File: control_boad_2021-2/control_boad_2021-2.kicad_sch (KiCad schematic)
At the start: 29 parts, among them J1 Conn_01x10_Female, J2 Conn_01x10_Female, J3 USB_C_Receptacle_PowerOnly_6P, J4 USB_C_Receptacle_PowerOnly_6P, J5 Conn_01x03_Female, U1 ESP32-DevKitC, U2 IM920s

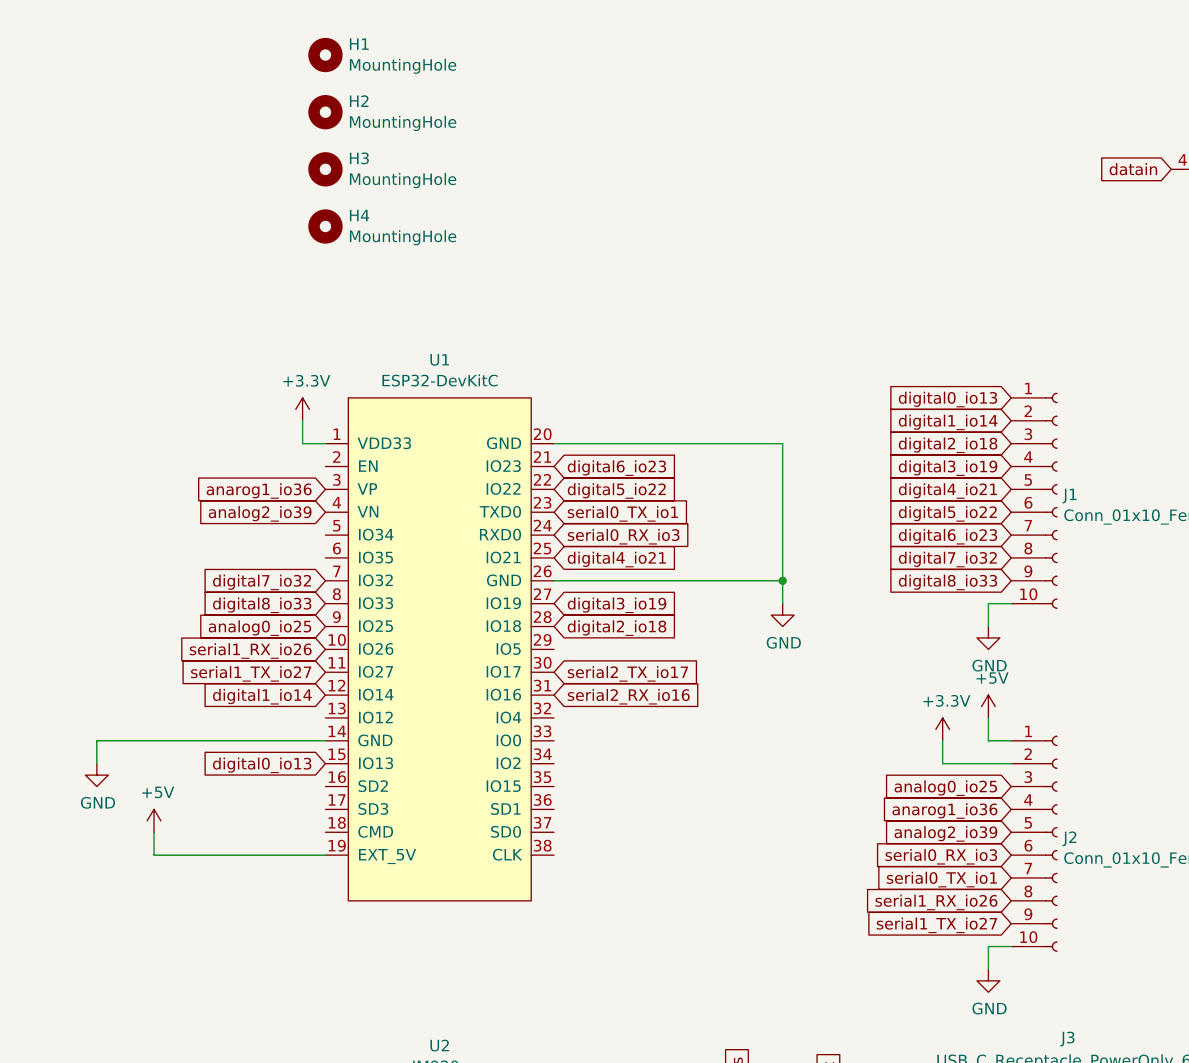
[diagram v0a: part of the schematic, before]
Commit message: replace esp32devkitc to doit esp32devkit v1
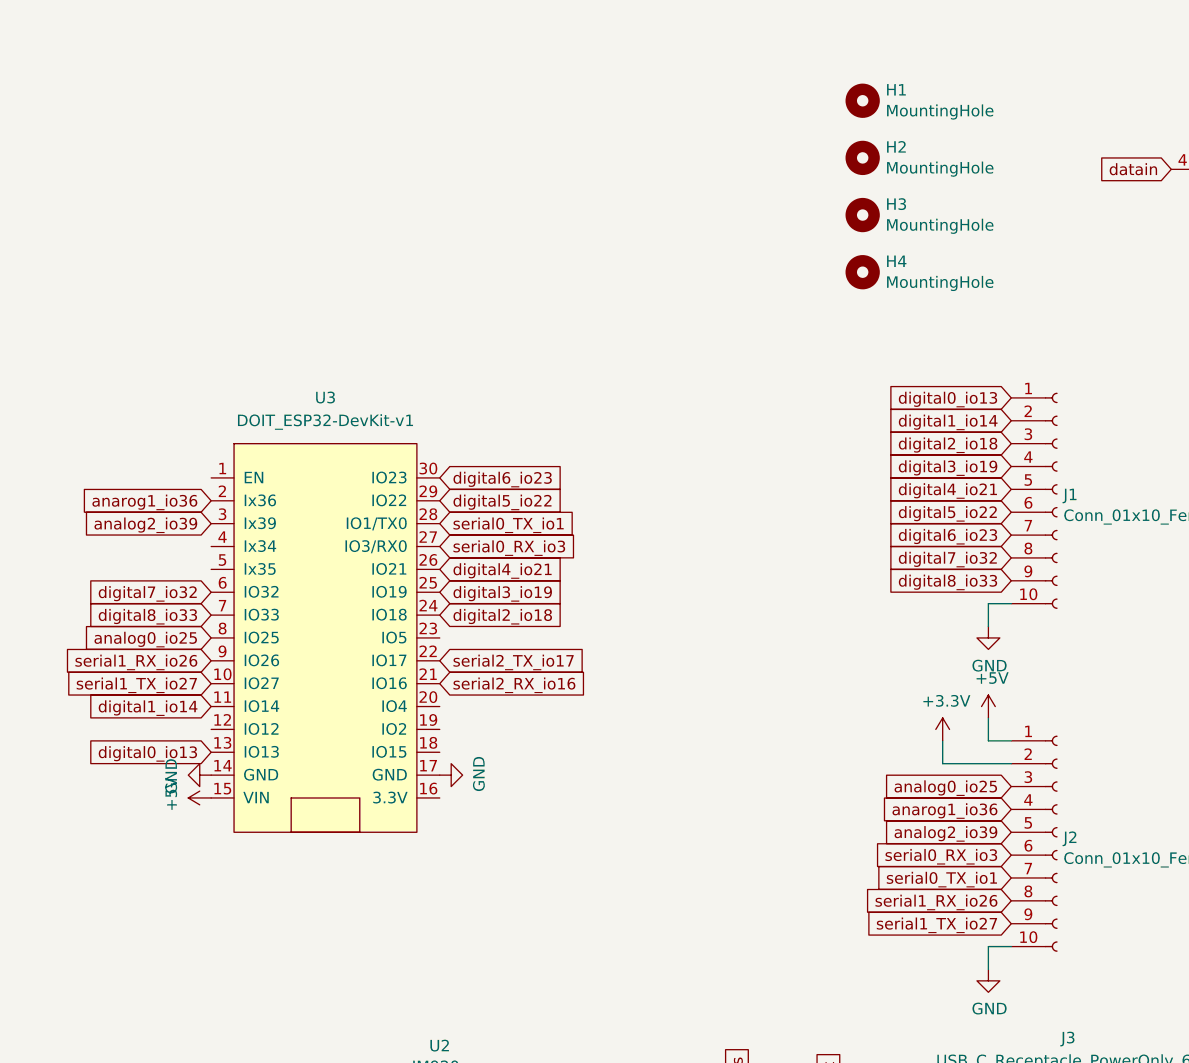
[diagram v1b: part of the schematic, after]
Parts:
- removed U1: ESP32-DevKitC, Boad_dev:ESP32-DevKitC, symbol Boad_dev:ESP32-DevKitC
- added U3: DOIT_ESP32-DevKit-v1, Boad_dev:DOIT_ESP32-DevKit-v1, symbol Boad_dev:DOIT_ESP32-DevKit-v1
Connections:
- net +5V: now also U3.15 (VIN)
- net GND: now also U3.14 (GND), U3.17 (GND)
- net analog0_io25: now also U3.8 (IO25)
- net analog2_io39: now also U3.3 (Ix39)
- net anarog1_io36: now also U3.2 (Ix36)
- net datain: now also U3.9 (IO26)
- net digital0_io13: now also U3.13 (IO13)
- net digital1_io14: now also U3.11 (IO14)
- net digital2_io18: now also U3.24 (IO18)
- net digital3_io19: now also U3.25 (IO19)
- net digital4_io21: now also U3.26 (IO21)
- net digital5_io22: now also U3.29 (IO22)
- net digital6_io23: now also U3.30 (IO23)
- net digital7_io32: now also U3.6 (IO32)
- net digital8_io33: now also U3.7 (IO33)
- net serial0_RX_io3: now also U3.27 (IO3/RX0)
- net serial0_TX_io1: now also U3.28 (IO1/TX0)
- net serial1_TX_io27: now also U3.10 (IO27)
- net serial2_RX_io16: now also U3.21 (IO16)
- net serial2_TX_io17: now also U3.22 (IO17)
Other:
- moved on the sheet: H1, H2, H3, H4
